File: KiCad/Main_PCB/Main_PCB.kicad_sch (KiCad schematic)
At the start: 50 parts, among them IC1 AP3602, J1 USB_C_Receptacle_USB2.0_14P, J3 Video Out, Q1 S8050, Q2 S8050, SW3 Main Power, U1 CP2102N-Axx-xQFN28, U2 ESP32-PICO-D4, U3 MCP73831-2-OT, U4 AMS1117

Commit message: Started PCB
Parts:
- BT1: footprint Connector_Wire:SolderWire-0.1sqmm_1x01_D0.4mm_OD1mm -> Connector_Wire:SolderWire-0.1sqmm_1x02_P3.6mm_D0.4mm_OD1mm
- C1, C10, C11, C12, C13, C14, C15, C2, C3, C4, C5, C6, C7, C8, C9: footprint Capacitor_SMD:C_1206_3216Metric -> Capacitor_SMD:C_0402_1005Metric
- GREEN1, RED1: footprint LED_THT:LED_D3.0mm -> LED_SMD:LED_0201_0603Metric
- R1, R12, R2: footprint Resistor_SMD:R_1206_3216Metric -> Resistor_SMD:R_0603_1608Metric
- R10, R11, R13, R14, R3, R4, R5, R6, R7, R8, R9: footprint Resistor_SMD:R_1206_3216Metric -> Resistor_SMD:R_0402_1005Metric
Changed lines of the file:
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@@
 			)
 		)
-		(property "Footprint" "Resistor_SMD:R_1206_3216Metric"
+		(property "Footprint" "Resistor_SMD:R_0603_1608Metric"
 			(at 26.416 192.024 90)
 			(effects
@@
 			)
 		)
-		(property "Footprint" "Resistor_SMD:R_1206_3216Metric"
+		(property "Footprint" "Resistor_SMD:R_0402_1005Metric"
 			(at 322.326 65.786 90)
 			(effects
@@
 			)
 		)
-		(property "Footprint" "Capacitor_SMD:C_1206_3216Metric"
+		(property "Footprint" "Capacitor_SMD:C_0402_1005Metric"
 			(at 281.6352 152.4 0)
 			(effects
@@
 			)
 		)
-		(property "Footprint" "Capacitor_SMD:C_1206_3216Metric"
+		(property "Footprint" "Capacitor_SMD:C_0402_1005Metric"
 			(at 72.39 75.8952 0)
 			(effects
@@
 			)
 		)
-		(property "Footprint" "Resistor_SMD:R_1206_3216Metric"
+		(property "Footprint" "Resistor_SMD:R_0402_1005Metric"
 			(at 42.926 92.964 90)
 			(effects
@@
 			)
 		)
-		(property "Footprint" "Capacitor_SMD:C_1206_3216Metric"
+		(property "Footprint" "Capacitor_SMD:C_0402_1005Metric"
 			(at 84.7852 59.69 0)
 			(effects
@@
 			)
 		)
-		(property "Footprint" "Resistor_SMD:R_1206_3216Metric"
+		(property "Footprint" "Resistor_SMD:R_0402_1005Metric"
 			(at 100.584 112.014 90)
 			(effects
@@
 			)
 		)
-		(property "Footprint" "Capacitor_SMD:C_1206_3216Metric"
+		(property "Footprint" "Capacitor_SMD:C_0402_1005Metric"
 			(at 42.8752 107.95 0)
 			(effects
@@
 			)
 		)
-		(property "Footprint" "Capacitor_SMD:C_1206_3216Metric"
+		(property "Footprint" "Capacitor_SMD:C_0402_1005Metric"
 			(at 68.2752 59.69 0)
 			(effects
@@
 			)
 		)
-		(property "Footprint" "Resistor_SMD:R_1206_3216Metric"
+		(property "Footprint" "Resistor_SMD:R_0402_1005Metric"
 			(at 321.056 87.884 90)
 			(effects
@@
 			)
 		)
-		(property "Footprint" "Resistor_SMD:R_1206_3216Metric"
+		(property "Footprint" "Resistor_SMD:R_0402_1005Metric"
 			(at 122.936 191.516 90)
 			(effects
@@
 			)
 		)
-		(property "Footprint" "Resistor_SMD:R_1206_3216Metric"
+		(property "Footprint" "Resistor_SMD:R_0603_1608Metric"
 			(at 26.416 205.994 90)
 			(effects
@@
 			)
 		)
-		(property "Footprint" "Capacitor_SMD:C_1206_3216Metric"
+		(property "Footprint" "Capacitor_SMD:C_0402_1005Metric"
 			(at 342.5952 203.2 0)
 			(effects
@@
 			)
 		)
-		(property "Footprint" "Capacitor_SMD:C_1206_3216Metric"
+		(property "Footprint" "Capacitor_SMD:C_0402_1005Metric"
 			(at 69.5452 85.09 0)
 			(effects
@@
 			)
 		)
-		(property "Footprint" "Connector_Wire:SolderWire-0.1sqmm_1x01_D0.4mm_OD1mm"
+		(property "Footprint" "Connector_Wire:SolderWire-0.1sqmm_1x02_P3.6mm_D0.4mm_OD1mm"
 			(at 362.966 74.93 90)
 			(effects
@@
 			)
 		)
-		(property "Footprint" "Resistor_SMD:R_1206_3216Metric"
+		(property "Footprint" "Resistor_SMD:R_0402_1005Metric"
 			(at 228.346 248.666 90)
 			(effects
@@
 			)
 		)
-		(property "Footprint" "Capacitor_SMD:C_1206_3216Metric"
+		(property "Footprint" "Capacitor_SMD:C_0402_1005Metric"
 			(at 337.5152 85.09 0)
 			(effects
@@
 			)
 		)
-		(property "Footprint" "Capacitor_SMD:C_1206_3216Metric"
+		(property "Footprint" "Capacitor_SMD:C_0402_1005Metric"
 			(at 156.21 244.8052 0)
 			(effects
@@
 			)
 		)
-		(property "Footprint" "Capacitor_SMD:C_1206_3216Metric"
+		(property "Footprint" "Capacitor_SMD:C_0402_1005Metric"
 			(at 74.93 169.2148 0)
 			(effects
@@
 			)
 		)
-		(property "Footprint" "Capacitor_SMD:C_1206_3216Metric"
+		(property "Footprint" "Capacitor_SMD:C_0402_1005Metric"
 			(at 304.8 54.3052 0)
 			(effects
@@
 			)
 		)
-		(property "Footprint" "Capacitor_SMD:C_1206_3216Metric"
+		(property "Footprint" "Capacitor_SMD:C_0402_1005Metric"
 			(at 355.2952 142.24 0)
 			(effects
@@
 			)
 		)
-		(property "Footprint" "LED_THT:LED_D3.0mm"
+		(property "Footprint" "LED_SMD:LED_0201_0603Metric"
 			(at 320.04 96.52 0)
 			(effects
@@
 			)
 		)
-		(property "Footprint" "Resistor_SMD:R_1206_3216Metric"
+		(property "Footprint" "Resistor_SMD:R_0402_1005Metric"
 			(at 122.936 204.216 90)
 			(effects
@@
 			)
 		)
-		(property "Footprint" "Resistor_SMD:R_1206_3216Metric"
+		(property "Footprint" "Resistor_SMD:R_0402_1005Metric"
 			(at 81.534 211.836 90)
 			(effects
@@
 			)
 		)
-		(property "Footprint" "Resistor_SMD:R_1206_3216Metric"
+		(property "Footprint" "Resistor_SMD:R_0402_1005Metric"
 			(at 289.306 87.884 90)
 			(effects
@@
 			)
 		)
-		(property "Footprint" "Resistor_SMD:R_1206_3216Metric"
+		(property "Footprint" "Resistor_SMD:R_0402_1005Metric"
 			(at 228.346 242.316 90)
 			(effects
@@
 			)
 		)
-		(property "Footprint" "Capacitor_SMD:C_1206_3216Metric"
+		(property "Footprint" "Capacitor_SMD:C_0402_1005Metric"
 			(at 107.95 244.8052 0)
 			(effects
@@
 			)
 		)
-		(property "Footprint" "Capacitor_SMD:C_1206_3216Metric"
+		(property "Footprint" "Capacitor_SMD:C_0402_1005Metric"
 			(at 304.4952 203.2 0)
 			(effects
@@
 			)
 		)
-		(property "Footprint" "Capacitor_SMD:C_1206_3216Metric"
+		(property "Footprint" "Capacitor_SMD:C_0402_1005Metric"
 			(at 295.91 133.0452 0)
 			(effects
@@
 			)
 		)
-		(property "Footprint" "Resistor_SMD:R_1206_3216Metric"
+		(property "Footprint" "Resistor_SMD:R_0603_1608Metric"
 			(at 309.626 162.306 90)
 			(effects
@@
 			)
 		)
-		(property "Footprint" "Resistor_SMD:R_1206_3216Metric"
+		(property "Footprint" "Resistor_SMD:R_0402_1005Metric"
 			(at 36.576 180.594 90)
 			(effects
@@
 			)
 		)
-		(property "Footprint" "LED_THT:LED_D3.0mm"
+		(property "Footprint" "LED_SMD:LED_0201_0603Metric"
 			(at 308.61 64.77 0)
 			(effects

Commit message: Changed Footprints
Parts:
- J1: footprint Connector_USB:USB_C_Receptacle_Amphenol_12401548E4-2A -> Connector_USB:USB_C_Receptacle_GCT_USB4085
- Q1, Q2: footprint Package_TO_SOT_THT:TO-92_Inline -> Package_TO_SOT_SMD:SOT-23
- SW3: footprint Button_Switch_SMD:SW_DIP_SPSTx01_Slide_6.7x4.1mm_W6.73mm_P2.54mm_LowProfile_JPin -> Button_Switch_SMD:SW_DIP_SPSTx01_Slide_Copal_CHS-01B_W7.62mm_P1.27mm
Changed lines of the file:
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@@
 			)
 		)
-		(property "Footprint" "Button_Switch_SMD:SW_DIP_SPSTx01_Slide_6.7x4.1mm_W6.73mm_P2.54mm_LowProfile_JPin"
+		(property "Footprint" "Button_Switch_SMD:SW_DIP_SPSTx01_Slide_Copal_CHS-01B_W7.62mm_P1.27mm"
 			(at 360.68 88.9 0)
 			(effects
@@
 			)
 		)
-		(property "Footprint" "Connector_USB:USB_C_Receptacle_Amphenol_12401548E4-2A"
+		(property "Footprint" "Connector_USB:USB_C_Receptacle_GCT_USB4085"
 			(at 191.77 190.5 0)
 			(effects
@@
 			)
 		)
-		(property "Footprint" "Package_TO_SOT_THT:TO-92_Inline"
+		(property "Footprint" "Package_TO_SOT_SMD:SOT-23"
 			(at 143.51 192.405 0)
 			(effects
@@
 		(on_board yes)
 		(dnp no)
-		(fields_autoplaced yes)
 		(property "Reference" "C14"
 			(at 345.44 198.1199 0)
@@
 				)
 				(justify left)
-				(hide yes)
 			)
 		)
 		(property "Value" "10uF"
-			(at 345.44 200.6599 0)
+			(at 345.694 200.152 0)
 			(effects
 				(font
@@
 			)
 		)
-		(property "Footprint" "Package_TO_SOT_THT:TO-92_Inline"
+		(property "Footprint" "Package_TO_SOT_SMD:SOT-23"
 			(at 143.51 201.295 0)
 			(effects

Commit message: PCB update
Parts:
- removed C10: 1uf, Capacitor_SMD:C_0402_1005Metric, symbol Device:C
- removed C15, C9: 10uF, Capacitor_SMD:C_0402_1005Metric, symbol Device:C
- removed IC1: AP3602, Package_TO_SOT_SMD:SOT-23-6, symbol Adafruit AP6302-eagle-import:AP3602
- removed J3: Video Out, Connector_Wire:SolderWire-0.1sqmm_1x01_D0.4mm_OD1mm, symbol Connector:Conn_01x01_Pin
- removed R12: 100K, Resistor_SMD:R_0603_1608Metric, symbol Device:R_US
- added J2: Display, Connector_Wire:SolderWire-0.1sqmm_1x04_P3.6mm_D0.4mm_OD1mm, symbol Connector:Conn_01x04_Socket
- GREEN1, RED1: footprint LED_SMD:LED_0201_0603Metric -> LED_SMD:LED_0402_1005Metric
- J1: footprint Connector_USB:USB_C_Receptacle_GCT_USB4085 -> Connector_USB:USB_C_Receptacle_GCT_USB4110
- L1: footprint Inductor_SMD:L_1206_3216Metric -> Inductor_SMD:L_0603_1608Metric
- renumbered C13 to C10, C14 to C11, C8 to C12, C6 to C4, C4 to C5, C5 to C6, C11 to C8, C12 to C9, R13 to R12, R14 to R13, R4 to R3, R3 to R4
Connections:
- net +3.3V: now also C11.1, U4.2 (VO), J2.2 (Pin_2)
- net +3.7V Bat: now also SW3.2 (B)
- net +5V USB: now also D3.1 (K)
- net GND: now also J2.1 (Pin_1)
- net SCL: now reaches U2.39 (IO22)
- net SCL: now also J2.3 (Pin_3)
- net SDA: now reaches U2.42 (IO21)
- net SDA: now also J2.4 (Pin_4)
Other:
- note removed: "Pump Charger"
- moved on the sheet: C11, C12, C7, C8, R10, R9, SW1, SW2, U4

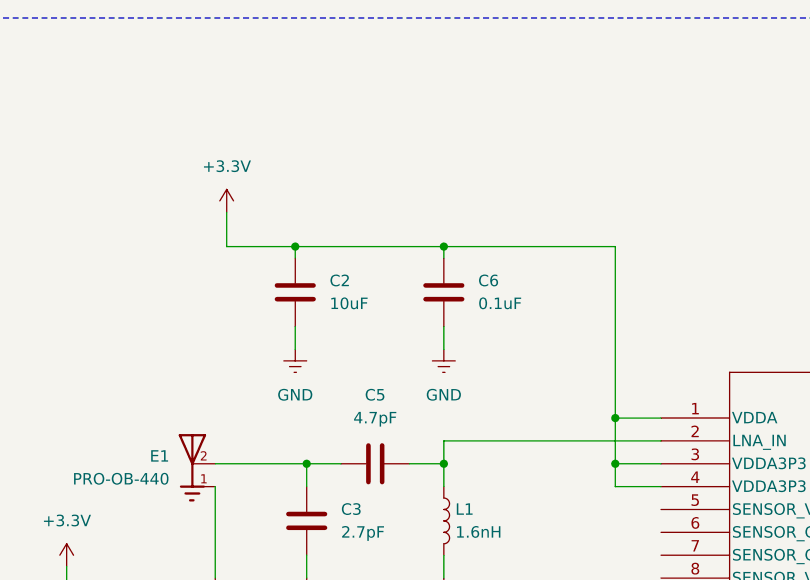
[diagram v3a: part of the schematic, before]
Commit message: Most traces done
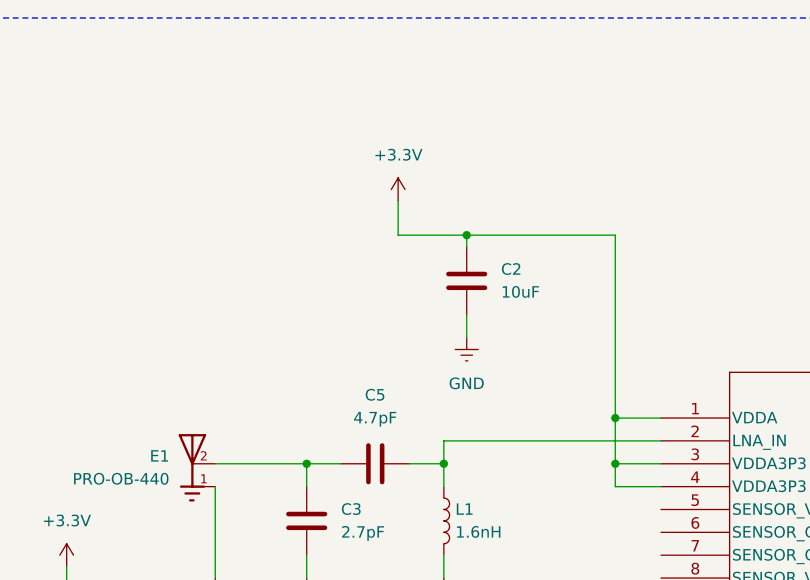
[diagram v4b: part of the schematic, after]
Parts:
- removed C6: 0.1uF, Capacitor_SMD:C_0402_1005Metric, symbol Device:C
- J1: footprint Connector_USB:USB_C_Receptacle_GCT_USB4110 -> Connector_USB:USB_C_Receptacle_GCT_USB4085
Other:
- moved on the sheet: C2
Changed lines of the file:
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@@
 	)
 	(junction
-		(at 67.31 50.8)
+		(at 86.36 49.53)
 		(diameter 0)
 		(color 0 0 0 0)
@@
 	)
 	(junction
-		(at 83.82 50.8)
-		(diameter 0)
-		(color 0 0 0 0)
-	)
-	(junction
 		(at 306.07 195.58)
 		(diameter 0)
@@
 	(wire
 		(pts
-			(xy 59.69 46.99) (xy 59.69 50.8)
+			(xy 78.74 45.72) (xy 78.74 49.53)
 		)
 		(stroke
@@
 	(wire
 		(pts
-			(xy 83.82 50.8) (xy 67.31 50.8)
+			(xy 86.36 49.53) (xy 102.87 49.53)
 		)
 		(stroke
@@
 	(wire
 		(pts
-			(xy 67.31 59.69) (xy 67.31 62.23)
+			(xy 86.36 58.42) (xy 86.36 60.96)
 		)
 		(stroke
@@
 	(wire
 		(pts
-			(xy 59.69 50.8) (xy 67.31 50.8)
+			(xy 78.74 49.53) (xy 86.36 49.53)
 		)
 		(stroke
@@
 	(wire
 		(pts
-			(xy 83.82 52.07) (xy 83.82 50.8)
-		)
-		(stroke
-			(width 0)
-			(type default)
-		)
-	)
-	(wire
-		(pts
 			(xy 180.34 69.85) (xy 173.99 69.85)
 		)
@@
 	(wire
 		(pts
-			(xy 67.31 50.8) (xy 67.31 52.07)
+			(xy 86.36 49.53) (xy 86.36 50.8)
 		)
 		(stroke
@@
 	(wire
 		(pts
-			(xy 83.82 59.69) (xy 83.82 62.23)
-		)
-		(stroke
-			(width 0)
-			(type default)
-		)
-	)
-	(wire
-		(pts
 			(xy 113.03 195.58) (xy 113.03 203.2)
 		)
@@
 	(wire
 		(pts
-			(xy 102.87 69.85) (xy 102.87 50.8)
+			(xy 102.87 69.85) (xy 102.87 49.53)
 		)
 		(stroke
@@
 	(wire
 		(pts
-			(xy 102.87 50.8) (xy 83.82 50.8)
-		)
-		(stroke
-			(width 0)
-			(type default)
-		)
-	)
-	(wire
-		(pts
 			(xy 298.45 53.34) (xy 304.8 53.34)
 		)
@@
 	)
 	(symbol
-		(lib_id "Device:C")
-		(at 83.82 55.88 0)
-		(unit 1)
-		(exclude_from_sim no)
-		(in_bom yes)
-		(on_board yes)
-		(dnp no)
-		(fields_autoplaced yes)
-		(property "Reference" "C6"
-			(at 87.63 54.6099 0)
-			(effects
-				(font
-					(size 1.27 1.27)
-				)
-				(justify left)
-			)
-		)
-		(property "Value" "0.1uF"
-			(at 87.63 57.1499 0)
-			(effects
-				(font
-					(size 1.27 1.27)
-				)
-				(justify left)
-			)
-		)
-		(property "Footprint" "Capacitor_SMD:C_0402_1005Metric"
-			(at 84.7852 59.69 0)
-			(effects
-				(font
-					(size 1.27 1.27)
-				)
-				(hide yes)
-			)
-		)
-		(property "Datasheet" "~"
-			(at 83.82 55.88 0)
-			(effects
-				(font
-					(size 1.27 1.27)
-				)
-				(hide yes)
-			)
-		)
-		(property "Description" "Unpolarized capacitor"
-			(at 83.82 55.88 0)
-			(effects
-				(font
-					(size 1.27 1.27)
-				)
-				(hide yes)
-			)
-		)
-		(pin "2"
-		)
-		(pin "1"
-		)
-		(instances
-			(project "Main_PCB"
-				(path "/a8c606a5-861f-4fc4-bc4f-8db124604f29"
-					(reference "C6")
-					(unit 1)
-				)
-			)
-		)
-	)
-	(symbol
 		(lib_id "Device:L")
 		(at 83.82 81.28 0)
@@
 	(symbol
 		(lib_id "Device:C")
-		(at 67.31 55.88 0)
+		(at 86.36 54.61 0)
 		(unit 1)
 		(exclude_from_sim no)
@@
 		(fields_autoplaced yes)
 		(property "Reference" "C2"
-			(at 71.12 54.6099 0)
+			(at 90.17 53.3399 0)
 			(effects
 				(font
@@
 		)
 		(property "Value" "10uF"
-			(at 71.12 57.1499 0)
+			(at 90.17 55.8799 0)
 			(effects
 				(font
@@
 		)
 		(property "Footprint" "Capacitor_SMD:C_0402_1005Metric"
-			(at 68.2752 59.69 0)
+			(at 87.3252 58.42 0)
 			(effects
 				(font
@@
 		)
 		(property "Datasheet" "~"
-			(at 67.31 55.88 0)
+			(at 86.36 54.61 0)
 			(effects
 				(font
@@
 		)
 		(property "Description" "Unpolarized capacitor"
-			(at 67.31 55.88 0)
+			(at 86.36 54.61 0)
 			(effects
 				(font
@@
 			)
 		)
-		(property "Footprint" "Connector_USB:USB_C_Receptacle_GCT_USB4110"
+		(property "Footprint" "Connector_USB:USB_C_Receptacle_GCT_USB4085"
 			(at 191.77 190.5 0)
 			(effects
@@
 	(symbol
 		(lib_id "power:GNDREF")
-		(at 67.31 62.23 0)
+		(at 86.36 60.96 0)
 		(unit 1)
 		(exclude_from_sim no)
@@
 		(fields_autoplaced yes)
 		(property "Reference" "#PWR010"
-			(at 67.31 68.58 0)
+			(at 86.36 67.31 0)
 			(effects
 				(font
@@
 		)
 		(property "Value" "GND"
-			(at 67.31 67.31 0)
+			(at 86.36 66.04 0)
 			(effects
 				(font
@@
 		)
 		(property "Footprint" ""
-			(at 67.31 62.23 0)
+			(at 86.36 60.96 0)
 			(effects
 				(font
@@
 		)
 		(property "Datasheet" ""
-			(at 67.31 62.23 0)
+			(at 86.36 60.96 0)
 			(effects
 				(font
@@
 		)
 		(property "Description" "Power symbol creates a global label with name \"GNDREF\" , reference supply ground"
-			(at 67.31 62.23 0)
+			(at 86.36 60.96 0)
 			(effects
 				(font
@@
 	(symbol
 		(lib_id "power:+3.3V")
-		(at 59.69 46.99 0)
+		(at 78.74 45.72 0)
 		(unit 1)
 		(exclude_from_sim no)
@@
 		(fields_autoplaced yes)
 		(property "Reference" "#PWR09"
-			(at 59.69 50.8 0)
+			(at 78.74 49.53 0)
 			(effects
 				(font
@@
 		)
 		(property "Value" "+3.3V"
-			(at 59.69 41.91 0)
+			(at 78.74 40.64 0)
 			(effects
 				(font
@@
 		)
 		(property "Footprint" ""
-			(at 59.69 46.99 0)
+			(at 78.74 45.72 0)
 			(effects
 				(font
@@
 		)
 		(property "Datasheet" ""
-			(at 59.69 46.99 0)
+			(at 78.74 45.72 0)
 			(effects
 				(font
@@
 		)
 		(property "Description" "Power symbol creates a global label with name \"+3.3V\""
-			(at 59.69 46.99 0)
+			(at 78.74 45.72 0)
 			(effects
 				(font
@@
 					(unit 1)
 				)
-			)
-		)
-	)
-	(symbol
-		(lib_id "power:GNDREF")
-		(at 83.82 62.23 0)
-		(unit 1)
-		(exclude_from_sim no)
-		(in_bom yes)
-		(on_board yes)
-		(dnp no)
-		(fields_autoplaced yes)
-		(property "Reference" "#PWR014"
-			(at 83.82 68.58 0)
-			(effects
-				(font
-					(size 1.27 1.27)
-				)
-				(hide yes)
-			)
-		)
-		(property "Value" "GND"
-			(at 83.82 67.31 0)
-			(effects
-				(font
-					(size 1.27 1.27)
-				)
-			)
-		)
-		(property "Footprint" ""
-			(at 83.82 62.23 0)
-			(effects
-				(font
-					(size 1.27 1.27)
-				)
-				(hide yes)
-			)
-		)
-		(property "Datasheet" ""
-			(at 83.82 62.23 0)
-			(effects
-				(font
-					(size 1.27 1.27)
-				)
-				(hide yes)
-			)
-		)
-		(property "Description" "Power symbol creates a global label with name \"GNDREF\" , reference supply ground"
-			(at 83.82 62.23 0)
-			(effects
-				(font
-					(size 1.27 1.27)
-				)
-				(hide yes)
-			)
-		)
-		(pin "1"
-		)
-		(instances
-			(project "Main_PCB"
-				(path "/a8c606a5-861f-4fc4-bc4f-8db124604f29"
-					(reference "#PWR014")
-					(unit 1)
-				)

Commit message: Different layout attempt
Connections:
- net EN: now also C1.1, R4.2, U2.9 (EN)
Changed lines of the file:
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@@
+	)
+	(label "EN"
+		(at 41.91 99.06 0)
+		(fields_autoplaced yes)
+		(effects
+			(font
+				(size 1.27 1.27)
+			)
+			(justify left bottom)
+		)
 	)
 	(label "EN"

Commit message: Added Ground plane and Migrated Libraries
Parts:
- SW3: footprint Button_Switch_SMD:SW_DIP_SPSTx01_Slide_Copal_CHS-01B_W7.62mm_P1.27mm -> Connector_Wire:SolderWire-0.1sqmm_1x02_P3.6mm_D0.4mm_OD1mm
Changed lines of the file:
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@@
 			)
 		)
-		(property "Footprint" "Button_Switch_SMD:SW_DIP_SPSTx01_Slide_Copal_CHS-01B_W7.62mm_P1.27mm"
+		(property "Footprint" "Connector_Wire:SolderWire-0.1sqmm_1x02_P3.6mm_D0.4mm_OD1mm"
 			(at 360.68 88.9 0)
 			(effects

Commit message: Pre JLC Check
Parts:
- removed C4: 0.1uF, Capacitor_SMD:C_0402_1005Metric, symbol Device:C
- J1: footprint Connector_USB:USB_C_Receptacle_GCT_USB4085 -> Connector_USB:USB_C_Receptacle_GCT_USB4110
- L1: footprint Inductor_SMD:L_0603_1608Metric -> Inductor_SMD:L_0402_1005Metric
- renumbered C12 to C10, C3 to C2, C5 to C3, C2 to C4, C7 to C5, C8 to C6, C9 to C7, C10 to C8, C11 to C9

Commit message: Updated for JLCPCB
- Added BOM
- Changed Diode footprints
- added JLC part numbers
- added cap touch pins
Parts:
- added J3: Cap Touch, Connector_Wire:SolderWire-0.1sqmm_1x02_P3.6mm_D0.4mm_OD1mm, symbol Connector:Conn_01x02_Socket
- C1, C10, C5: LCSC (none) -> C141382
- C2: LCSC (none) -> C172851
- C3: LCSC (none) -> C85883
- C4, C6, C7, C8, C9: LCSC (none) -> C87148
- D1, D2, D4: footprint Diode_SMD:D_SOD-923 -> Diode_SMD:D_SOD-523; LCSC (none) -> C5246195
- D3: footprint Diode_SMD:D_SOD-923 -> Diode_SMD:D_SOD-323; LCSC (none) -> C124187
- E1: LCSC (none) -> C5122736
- GREEN1: LCSC (none) -> C434449
- J1: footprint Connector_USB:USB_C_Receptacle_GCT_USB4110 -> Connector_USB:USB_C_Receptacle_GCT_USB4085; LCSC (none) -> C9900013983
- L1: LCSC (none) -> C279912
- Q1, Q2: LCSC (none) -> C909746
- R1: LCSC (none) -> C25961
- R10, R9: LCSC (none) -> C138287
- R11, R12, R4, R5, R6, R7, R8: LCSC (none) -> C25744
- R13, R3: LCSC (none) -> C100608
- R2: LCSC (none) -> C23061
- RED1: LCSC (none) -> C434445
- SW1, SW2: LCSC (none) -> C115357
- U1: LCSC (none) -> C1550553
- U2: LCSC (none) -> C193707
- U3: LCSC (none) -> C424093
- U4: LCSC (none) -> C6186
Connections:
- net at U2.10 (IO34): now also J3.2 (Pin_2)
- net at U2.11 (IO35): now also J3.1 (Pin_1)
